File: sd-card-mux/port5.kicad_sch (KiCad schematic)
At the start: 10 parts, among them J201 47309-2285, U201 74LVC1G3157, U202 74LVC1G3157, U203 74LVC1G3157, U204 74LVC1G3157, U205 74LVC1G3157, U206 74LVC1G3157

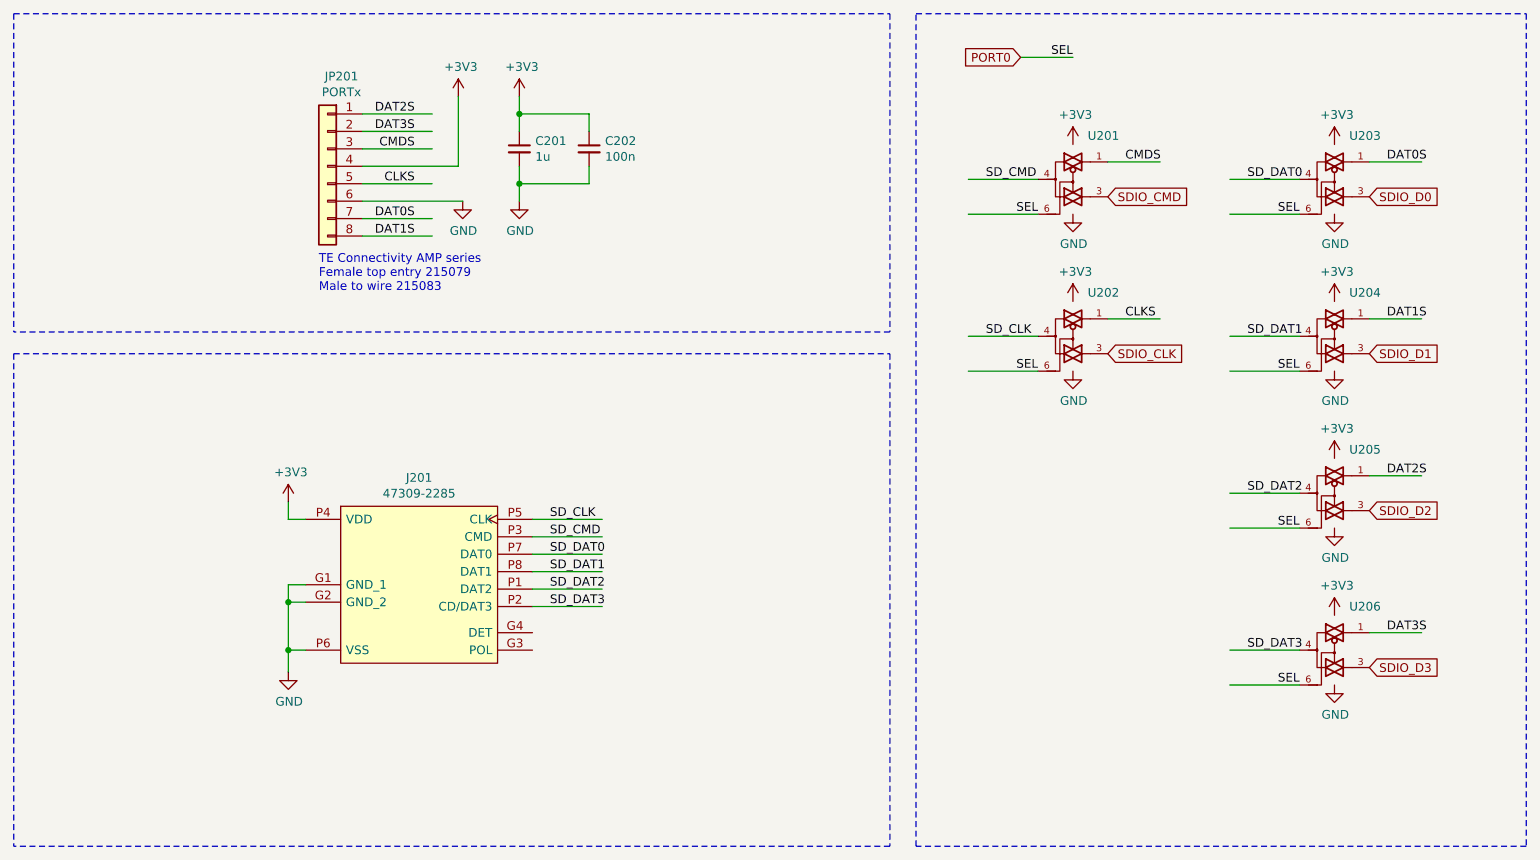
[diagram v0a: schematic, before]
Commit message: Added MCP23008 alternative
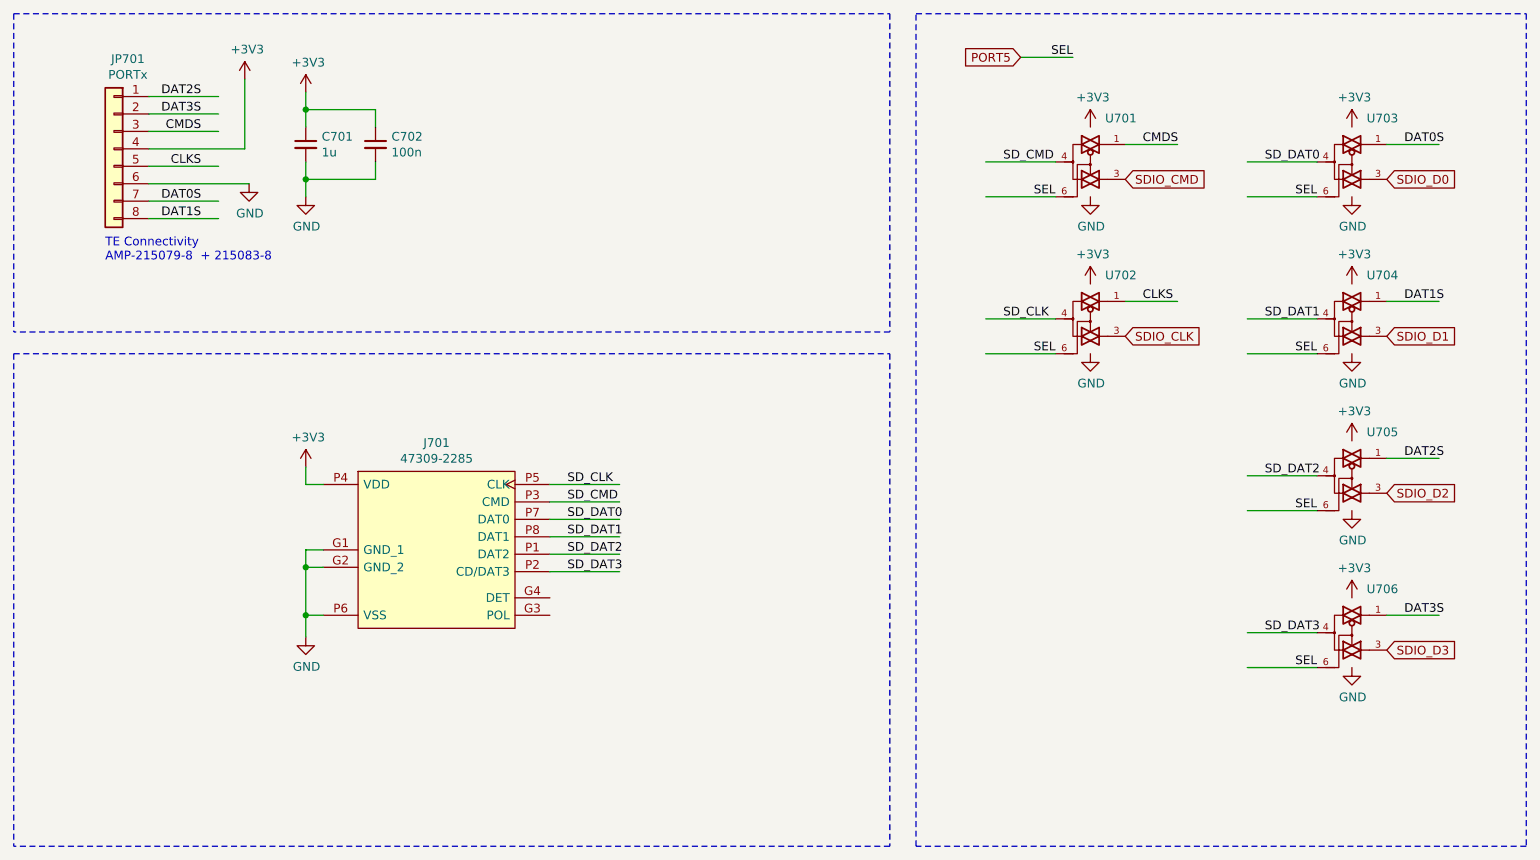
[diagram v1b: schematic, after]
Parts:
- removed C201: 1u, Capacitor_SMD:C_0402_1005Metric, symbol Device:C_Small
- removed C202: 100n, Capacitor_SMD:C_0402_1005Metric, symbol Device:C_Small
- removed J201: 47309-2285, footprints:47309-2285, symbol 47309-2285:47309-2285
- removed JP201: PORTx, Connector_JST:JST_PH_S8B-PH-K_1x08_P2.00mm_Horizontal, symbol Connector_Generic:Conn_01x08
- removed U201, U202, U203, U204, U205, U206: 74LVC1G3157, Package_TO_SOT_SMD:SOT-363_SC-70-6, symbol 74LVC1G3157:74LVC1G3157
- added C701: 1u, Capacitor_SMD:C_0402_1005Metric, symbol Device:C_Small
- added C702: 100n, Capacitor_SMD:C_0402_1005Metric, symbol Device:C_Small
- added J701: 47309-2285, footprints:47309-2285, symbol 47309-2285:47309-2285
- added JP701: PORTx, Connector_JST:JST_PH_S8B-PH-K_1x08_P2.00mm_Horizontal, symbol Connector_Generic:Conn_01x08
- added U701, U702, U703, U704, U705, U706: 74LVC1G3157, Package_TO_SOT_SMD:SOT-363_SC-70-6, symbol 74LVC1G3157:74LVC1G3157
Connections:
- net +3V3: now also C701.1, C702.1, J701.P4 (VDD), JP701.4 (Pin_4), U701.5 (VCC), U702.5 (VCC), U703.5 (VCC), U704.5 (VCC), U705.5 (VCC), U706.5 (VCC)
- net CLKS: now also JP701.5 (Pin_5), U702.1
- net CMDS: now also JP701.3 (Pin_3), U701.1
- net DAT0S: now also JP701.7 (Pin_7), U703.1
- net DAT1S: now also JP701.8 (Pin_8), U704.1
- net DAT2S: now also JP701.1 (Pin_1), U705.1
- net DAT3S: now also JP701.2 (Pin_2), U706.1
- net GND: now also C701.2, C702.2, J701.G1 (GND_1), J701.G2 (GND_2), J701.P6 (VSS), JP701.6 (Pin_6), U701.2 (GND), U702.2 (GND), U703.2 (GND), U704.2 (GND), U705.2 (GND), U706.2 (GND)
- net SDIO_CLK: now also U702.3
- net SDIO_CMD: now also U701.3
- net SDIO_D0: now also U703.3
- net SDIO_D1: now also U704.3
- net SDIO_D2: now also U705.3
- net SDIO_D3: now also U706.3
- net SD_CLK: now also J701.P5 (CLK), U702.4
- net SD_CMD: now also J701.P3 (CMD), U701.4
- net SD_DAT0: now also J701.P7 (DAT0), U703.4
- net SD_DAT1: now also J701.P8 (DAT1), U704.4
- net SD_DAT2: now also J701.P1 (DAT2), U705.4
- net SD_DAT3: now also J701.P2 (CD/DAT3), U706.4
- new net PORT5: U701.6, U702.6, U703.6, U704.6, U705.6, U706.6
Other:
- note added: "TE Connectivity AMP-215079-8 + 215083-8"
- note removed: "TE Connectivity AMP series Female top entry 215079 Male to wire 215083"

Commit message: Addedd missing upload port
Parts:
- C701: LCSC Part# (none) -> C52923
- C702: LCSC Part# (none) -> C1525
- JP701: footprint Connector_JST:JST_PH_S8B-PH-K_1x08_P2.00mm_Horizontal -> footprints:ConnectorMicromatch-8
- U701, U702, U703, U704, U705, U706: LCSC Part# (none) -> C38663
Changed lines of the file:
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@@
+      (effects (font (size 1.27 1.27)) hide)
+    )
+    (property "LCSC Part#" "C52923" (id 4) (at 63.5 38.1 0)
       (effects (font (size 1.27 1.27)) hide)
     )
@@
       (effects (font (size 1.27 1.27)) hide)
     )
+    (property "LCSC Part#" "C1525" (id 4) (at 73.66 38.1 0)
+      (effects (font (size 1.27 1.27)) hide)
+    )
   )
   (symbol (lib_name "74LVC1G3157:74LVC1G3157_2") (lib_id "74LVC1G3157:74LVC1G3157") (at 177.8 40.64 0) (unit 1)
@@
     )
     (property "Datasheet" "https://www.ti.com/lit/ds/symlink/sn74lvc1g3157.pdf" (id 3) (at 177.8 40.64 0)
+      (effects (font (size 1.27 1.27)) hide)
+    )
+    (property "LCSC Part#" " C38663" (id 4) (at 177.8 40.64 0)
       (effects (font (size 1.27 1.27)) hide)
     )
@@
       (effects (font (size 1.27 1.27)) hide)
     )
+    (property "LCSC Part#" " C38663" (id 4) (at 177.8 63.5 0)
+      (effects (font (size 1.27 1.27)) hide)
+    )
   )
   (symbol (lib_id "74LVC1G3157:74LVC1G3157") (at 215.9 40.64 0) (unit 1)
@@
     )
     (property "Datasheet" "https://www.ti.com/lit/ds/symlink/sn74lvc1g3157.pdf" (id 3) (at 215.9 40.64 0)
+      (effects (font (size 1.27 1.27)) hide)
+    )
+    (property "LCSC Part#" " C38663" (id 4) (at 215.9 40.64 0)
       (effects (font (size 1.27 1.27)) hide)
     )
@@
       (effects (font (size 1.27 1.27)) hide)
     )
+    (property "LCSC Part#" " C38663" (id 4) (at 215.9 63.5 0)
+      (effects (font (size 1.27 1.27)) hide)
+    )
   )
   (symbol (lib_id "74LVC1G3157:74LVC1G3157") (at 215.9 86.36 0) (unit 1)
@@
     )
     (property "Datasheet" "https://www.ti.com/lit/ds/symlink/sn74lvc1g3157.pdf" (id 3) (at 215.9 86.36 0)
+      (effects (font (size 1.27 1.27)) hide)
+    )
+    (property "LCSC Part#" " C38663" (id 4) (at 215.9 86.36 0)
       (effects (font (size 1.27 1.27)) hide)
     )
@@
       (effects (font (size 1.27 1.27)) hide)
     )
+    (property "LCSC Part#" " C38663" (id 4) (at 215.9 109.22 0)
+      (effects (font (size 1.27 1.27)) hide)
+    )
   )
   (symbol (lib_id "Connector_Generic:Conn_01x08") (at 35.56 38.735 0) (mirror y) (unit 1)
@@
     (property "Reference" "JP701" (id 0) (at 37.592 25.635 0))
     (property "Value" "PORTx" (id 1) (at 37.592 27.9335 0))
-    (property "Footprint" "Connector_JST:JST_PH_S8B-PH-K_1x08_P2.00mm_Horizontal" (id 2) (at 35.56 38.735 0)
+    (property "Footprint" "footprints:ConnectorMicromatch-8" (id 2) (at 35.56 38.735 0)
       (effects (font (size 1.27 1.27)) hide)
     )

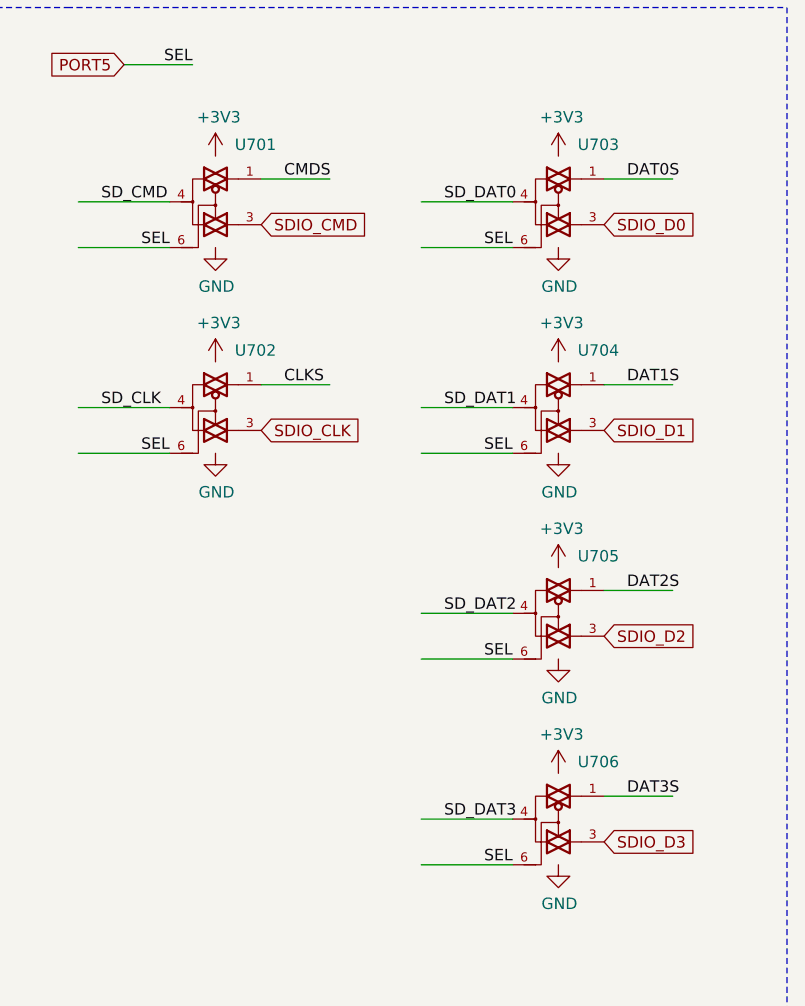
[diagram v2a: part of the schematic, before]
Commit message: Correction of inverted pins
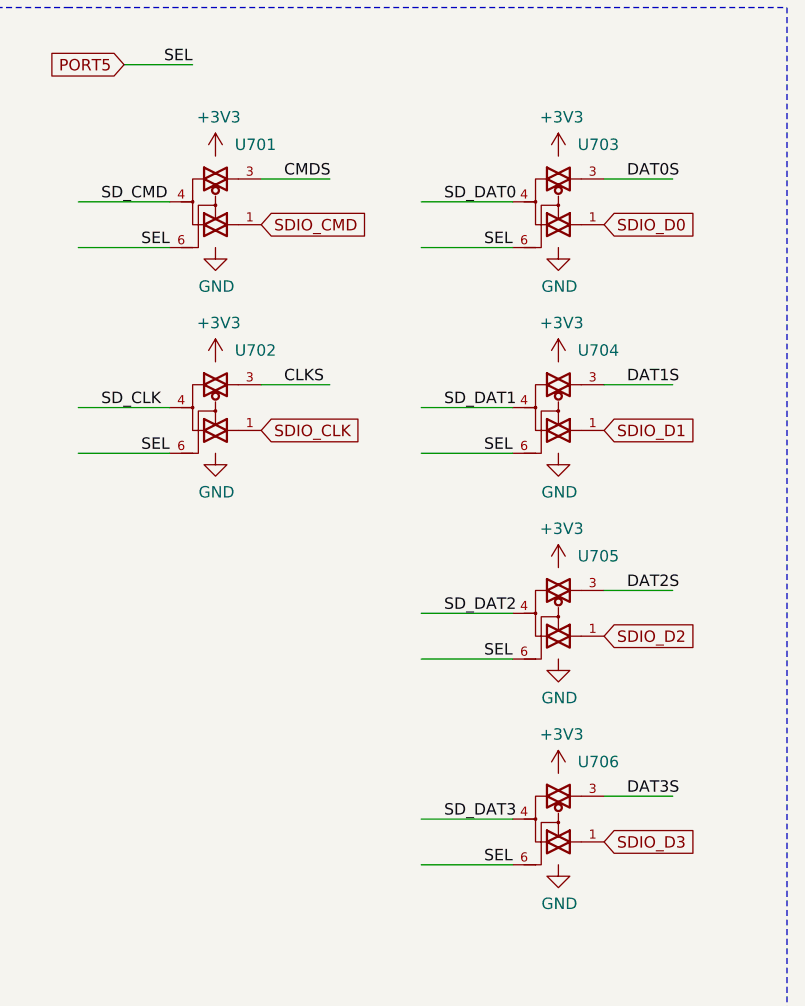
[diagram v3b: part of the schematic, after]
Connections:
- net CLKS: now also U702.3; no longer U702.1
- net CMDS: now also U701.3; no longer U701.1
- net DAT0S: now also U703.3; no longer U703.1
- net DAT1S: now also U704.3; no longer U704.1
- net DAT2S: now also U705.3; no longer U705.1
- net DAT3S: now also U706.3; no longer U706.1
- net SDIO_CLK: now also U702.1; no longer U702.3
- net SDIO_CMD: now also U701.1; no longer U701.3
- net SDIO_D0: now also U703.1; no longer U703.3
- net SDIO_D1: now also U704.1; no longer U704.3
- net SDIO_D2: now also U705.1; no longer U705.3
- net SDIO_D3: now also U706.1; no longer U706.3
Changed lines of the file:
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@@
 (kicad_sch (version 20200608) (host eeschema "(5.99.0-1973-g8c57821e9)")
-  (page 1 9)
+  (page 7 9)
   (paper "A4")
   (junction (at 63.5 33.02))
@@
     )
   )
-  (symbol (lib_id "74LVC1G3157:74LVC1G3157") (at 177.8 63.5 0) (unit 1)
+  (symbol (lib_name "74LVC1G3157:74LVC1G3157_1") (lib_id "74LVC1G3157:74LVC1G3157") (at 177.8 63.5 0) (unit 1)
     (in_bom yes) (on_board yes)
     (property "Reference" "U702" (id 0) (at 182.245 57.15 0))
@@
     )
   )
-  (symbol (lib_id "74LVC1G3157:74LVC1G3157") (at 215.9 40.64 0) (unit 1)
+  (symbol (lib_name "74LVC1G3157:74LVC1G3157_3") (lib_id "74LVC1G3157:74LVC1G3157") (at 215.9 40.64 0) (unit 1)
     (in_bom yes) (on_board yes)
     (property "Reference" "U703" (id 0) (at 220.345 34.29 0))
@@
     )
   )
-  (symbol (lib_id "74LVC1G3157:74LVC1G3157") (at 215.9 63.5 0) (unit 1)
+  (symbol (lib_name "74LVC1G3157:74LVC1G3157_4") (lib_id "74LVC1G3157:74LVC1G3157") (at 215.9 63.5 0) (unit 1)
     (in_bom yes) (on_board yes)
     (property "Reference" "U704" (id 0) (at 220.345 57.15 0))
@@
     )
   )
-  (symbol (lib_id "74LVC1G3157:74LVC1G3157") (at 215.9 86.36 0) (unit 1)
+  (symbol (lib_name "74LVC1G3157:74LVC1G3157_5") (lib_id "74LVC1G3157:74LVC1G3157") (at 215.9 86.36 0) (unit 1)
     (in_bom yes) (on_board yes)
     (property "Reference" "U705" (id 0) (at 220.345 80.01 0))

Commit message: Removal of host port and preparation for manufacturing
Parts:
- J701: Mechanical (none) -> T
- JP701: Mechanical (none) -> T; TME Part# (none) -> MM2x5
- U701, U702, U703, U704, U705, U706: LCSC Part# C38663 -> C265126; Rotation (none) -> 0
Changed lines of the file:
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@@
       (effects (font (size 1.27 1.27)) hide)
     )
-    (property "LCSC Part#" " C38663" (id 4) (at 177.8 40.64 0)
+    (property "LCSC Part#" "C265126" (id 4) (at 177.8 40.64 0)
+      (effects (font (size 1.27 1.27)) hide)
+    )
+    (property "Rotation" "0" (id 4) (at 177.8 40.64 0)
       (effects (font (size 1.27 1.27)) hide)
     )
@@
       (effects (font (size 1.27 1.27)) hide)
     )
-    (property "LCSC Part#" " C38663" (id 4) (at 177.8 63.5 0)
+    (property "LCSC Part#" "C265126" (id 4) (at 177.8 63.5 0)
+      (effects (font (size 1.27 1.27)) hide)
+    )
+    (property "Rotation" "0" (id 4) (at 177.8 63.5 0)
       (effects (font (size 1.27 1.27)) hide)
     )
@@
       (effects (font (size 1.27 1.27)) hide)
     )
-    (property "LCSC Part#" " C38663" (id 4) (at 215.9 40.64 0)
+    (property "LCSC Part#" "C265126" (id 4) (at 215.9 40.64 0)
+      (effects (font (size 1.27 1.27)) hide)
+    )
+    (property "Rotation" "0" (id 4) (at 215.9 40.64 0)
       (effects (font (size 1.27 1.27)) hide)
     )
@@
       (effects (font (size 1.27 1.27)) hide)
     )
-    (property "LCSC Part#" " C38663" (id 4) (at 215.9 63.5 0)
+    (property "LCSC Part#" "C265126" (id 4) (at 215.9 63.5 0)
+      (effects (font (size 1.27 1.27)) hide)
+    )
+    (property "Rotation" "0" (id 4) (at 215.9 63.5 0)
       (effects (font (size 1.27 1.27)) hide)
     )
@@
       (effects (font (size 1.27 1.27)) hide)
     )
-    (property "LCSC Part#" " C38663" (id 4) (at 215.9 86.36 0)
+    (property "LCSC Part#" "C265126" (id 4) (at 215.9 86.36 0)
+      (effects (font (size 1.27 1.27)) hide)
+    )
+    (property "Rotation" "0" (id 4) (at 215.9 86.36 0)
       (effects (font (size 1.27 1.27)) hide)
     )
@@
       (effects (font (size 1.27 1.27)) hide)
     )
-    (property "LCSC Part#" " C38663" (id 4) (at 215.9 109.22 0)
+    (property "LCSC Part#" "C265126" (id 4) (at 215.9 109.22 0)
+      (effects (font (size 1.27 1.27)) hide)
+    )
+    (property "Rotation" "0" (id 4) (at 215.9 109.22 0)
       (effects (font (size 1.27 1.27)) hide)
     )
@@
     )
     (property "Datasheet" "~" (id 3) (at 35.56 38.735 0)
+      (effects (font (size 1.27 1.27)) hide)
+    )
+    (property "TME Part#" "MM2x5" (id 4) (at 35.56 38.735 0)
+      (effects (font (size 1.27 1.27)) hide)
+    )
+    (property "Mechanical" "T" (id 4) (at 35.56 38.735 0)
       (effects (font (size 1.27 1.27)) hide)
     )
@@
       (effects (font (size 1.27 1.27)) (justify left) hide)
     )
+    (property "Mechanical" "T" (id 4) (at 66.04 88.265 0)
+      (effects (font (size 1.27 1.27)) hide)
+    )
   )
